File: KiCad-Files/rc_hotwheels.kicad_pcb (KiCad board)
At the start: 2 copper layers, 30 x 26 mm, 22 parts, among them IC1 BD6211F-E2, IC2 MIC5504-3.3YM5-TR, U1 STM32F070F6P6, U3 NRF24L01_Breakout

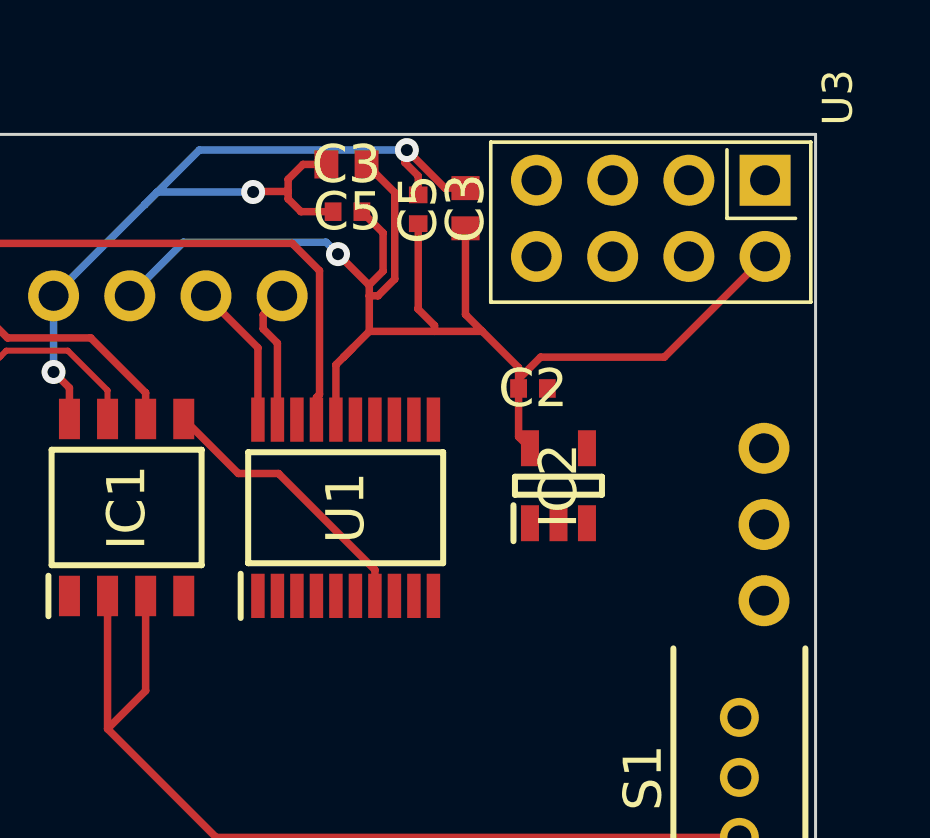
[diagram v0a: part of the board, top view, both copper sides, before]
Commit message: PCB Design
Connecting the Transceiver
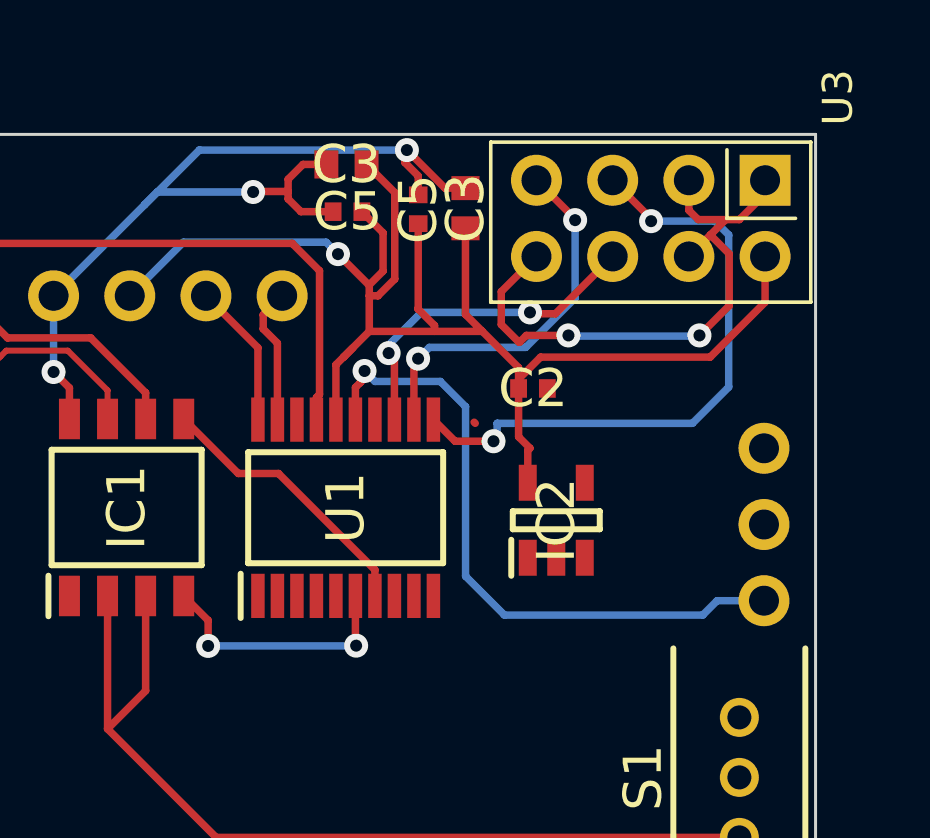
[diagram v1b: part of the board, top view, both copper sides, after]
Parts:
- moved IC2 1.15 mm to (126.0, 73.5)
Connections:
- IC1 pad 4: PA0 -> FIN
- U3 pad 5: PA5 -> SCK
- U3 pad 6: PA7 -> MOSI
- U3 pad 7: PA6 -> MISO
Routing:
- net GND: track 31.1 -> 73.0 mm, vias 3 -> 6
- net SCK: track 0.00 -> 21.0 mm, vias 0 -> 2
- net MISO: track 0.00 -> 13.0 mm, vias 0 -> 2
- net MOSI: track 0.00 -> 11.3 mm, vias 0 -> 2
- net FIN: track 0.00 -> 8.61 mm, vias 0 -> 2
- net VR_OUT: track 49.0 -> 51.0 mm

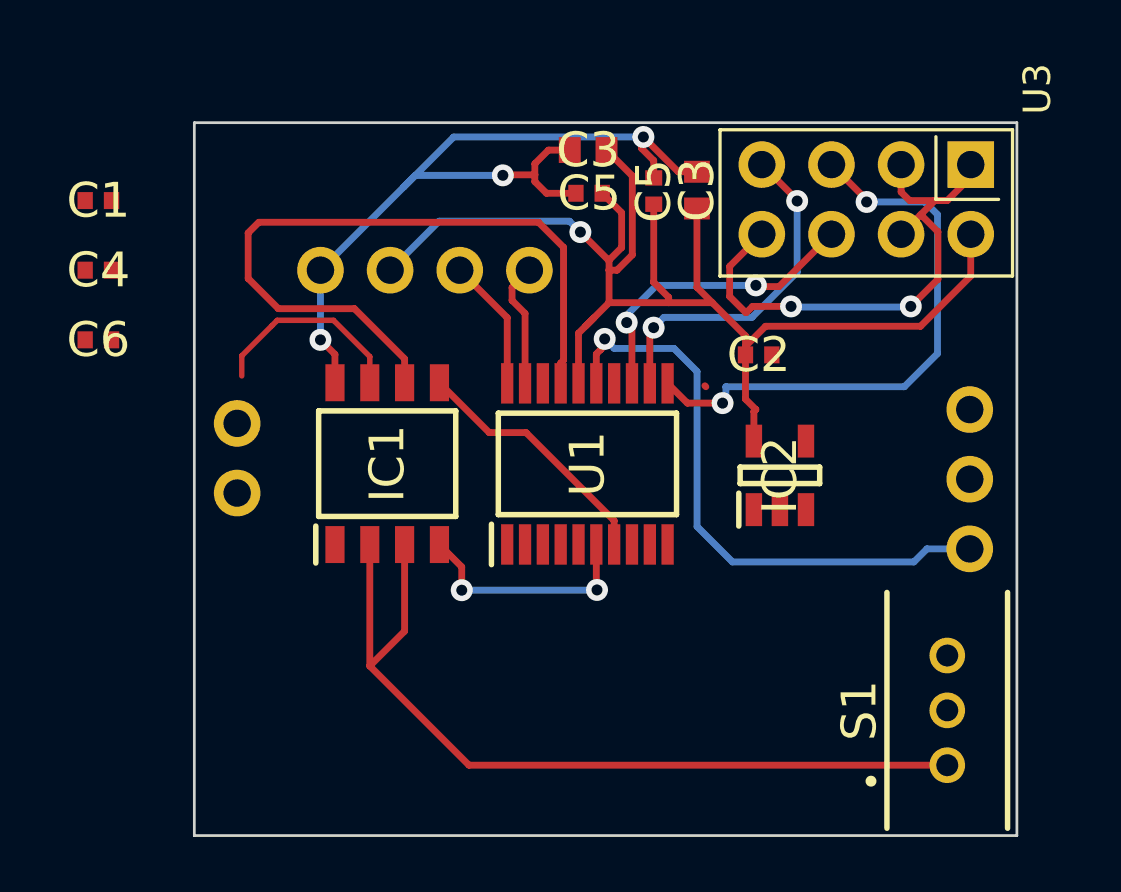
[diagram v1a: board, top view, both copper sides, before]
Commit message: Fixed all schematic errors.
Co-Authored-By: Yazid Almazroua <98489302+yazidta@users.noreply.github.com>
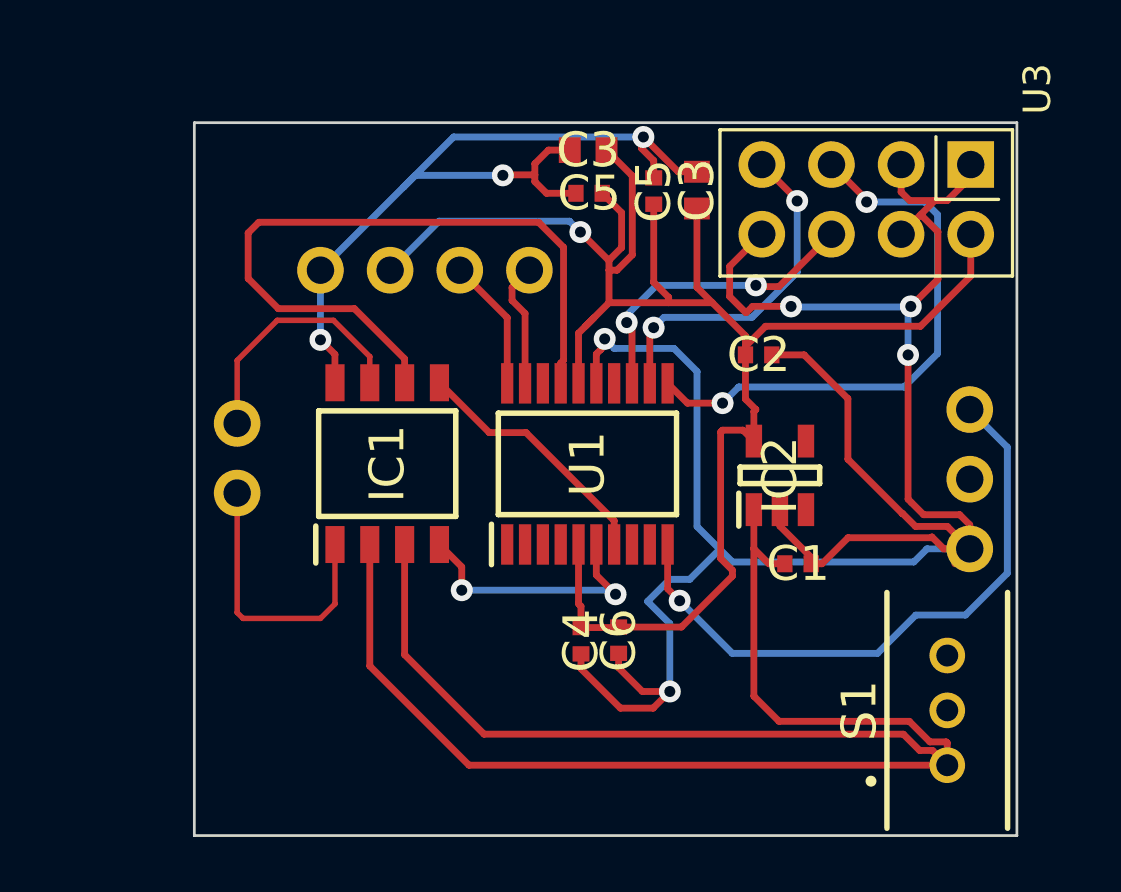
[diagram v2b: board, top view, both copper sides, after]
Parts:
- moved C1 28.8 mm to (126.6, 76.7), turned to 180 degrees
- moved C4 22.2 mm to (118.7, 79.6), turned to -90 degrees
- moved C6 21.9 mm to (120.1, 79.5), turned to 90 degrees
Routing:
- net GND: track 73.0 -> 119.1 mm, vias 6 -> 8
- net VCC: track 31.9 -> 69.2 mm
- net PWM: track 0.00 -> 22.7 mm, vias 0 -> 1
- net VR_OUT: track 51.0 -> 67.3 mm
- net Motor +: track 0.00 -> 10.4 mm
- net Motor -: track 7.44 -> 9.24 mm
- net FIN: track 8.61 -> 9.78 mm

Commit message: PCB V2.0
Co-Authored-By: Yazid Almazroua <98489302+yazidta@users.noreply.github.com>
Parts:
- removed ? (x9): , 
- removed the C3 at (123.0, 63.1)
- removed the C3 at (119.0, 61.7)
- removed the C5 at (119.0, 63.2)
- removed the C5 at (121.4, 63.2)
- added BT1: Battery_Cell, Library:Battery_Pads, F.Cu at (85.9, 51.3)
- added C3: 4.7uF, C4.7uF:CAPC1608X87N, F.Cu at (64.0, 43.7)
- added C5: 100nF, C100nF:CAPC1005X55N, F.Cu at (62.5, 43.9)
- added CH: Li-Ion 18650 battery charging, Library:Battery_Pads, F.Cu at (85.8, 56.9)
- added M1: Motor_Connection, Library:Motor_Connection, F.Cu at (85.9, 45.3)
- added SM1: Motor_Servo, Library:Servo_Motor, F.Cu at (59.8, 53.4)
- added ST: ST_Link, Library:ST_Link, F.Cu at (81.1, 35.3)
- S1: moved to B.Cu
- moved U3 76.6 mm to (60.1, 38.3), turned to 90 degrees
- moved C2 63.1 mm to (64.8, 50.7), turned to -90 degrees
- moved IC2 62.6 mm to (67.8, 50.2), turned to 180 degrees
- moved C1 61.4 mm to (71.0, 50.7), turned to -90 degrees
- moved S1 61.0 mm to (78.2, 53.3), turned to 0 degrees
- moved U1 57.9 mm to (69.0, 43.8), turned to 180 degrees
- moved C4 56.0 mm to (74.0, 46.0), turned to 90 degrees
- moved C6 55.8 mm to (75.5, 46.0), turned to -90 degrees
- moved IC1 43.5 mm to (80.6, 42.6), turned to -90 degrees
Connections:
- net VREF renamed Motor Speed
- C1 pad 1: GND -> Net-(IC2-GND)
- C2 pad 1: GND -> Net-(C2-Pad1)
- IC1 pad 4: FIN -> Motor Forward
- IC1 pad 5: RIN -> Motor Reverse
- IC2 pad 2: GND -> Net-(IC2-GND)
- S1 pad 2: +BATT -> Net-(BT1-+)
- U1 pad 6: FIN -> Motor Reverse
- U1 pad 7: RIN -> Motor Forward
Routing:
- net GND: track 119.1 -> 12.8 mm, vias 8 -> 4
- net VR_OUT: track 67.3 -> 45.2 mm, vias 1 -> 0
- net VCC: track 69.2 -> 48.9 mm
- net SCK: track 20.6 -> 2.99 mm, vias 2 -> 0
- net SYS_SWCLK: track 4.84 -> 16.8 mm
- net Motor Forward: track 0.00 -> 10.7 mm, vias 0 -> 2
- net FIN: track 9.78 -> 0.00 mm, vias 2 -> 0
- net RIN: track 9.32 -> 0.00 mm
- net Net-(BT1-+): track 0.00 -> 9.30 mm
- net SYS_SWDIO: track 4.59 -> 13.7 mm
- net Motor Reverse: track 0.00 -> 8.90 mm, vias 0 -> 2
- net MISO: track 13.0 -> 4.86 mm, vias 2 -> 0
- net Net-(S3-BATT+): track 0.00 -> 7.94 mm
- net Motor Speed: track 26.5 -> 21.9 mm, vias 0 -> 2
- net Motor +: track 10.4 -> 7.03 mm
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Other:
- board size 30 x 26 mm -> 29.5 x 23.5 mm

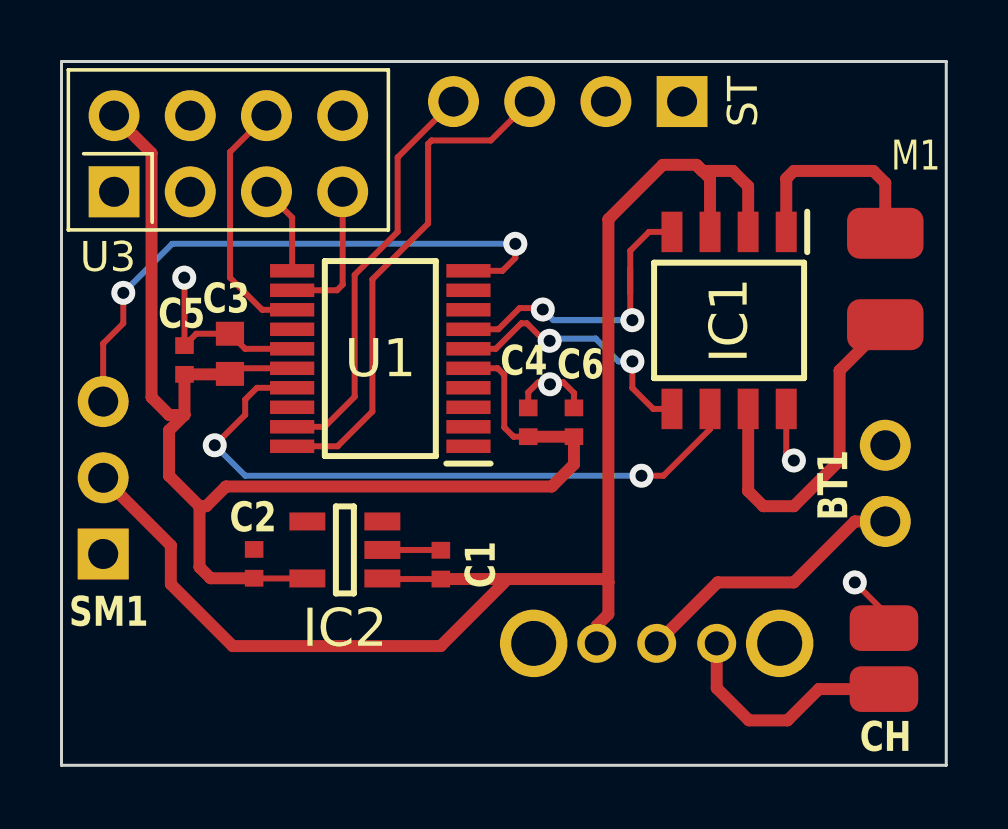
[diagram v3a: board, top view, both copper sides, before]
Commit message: Updated all power traces
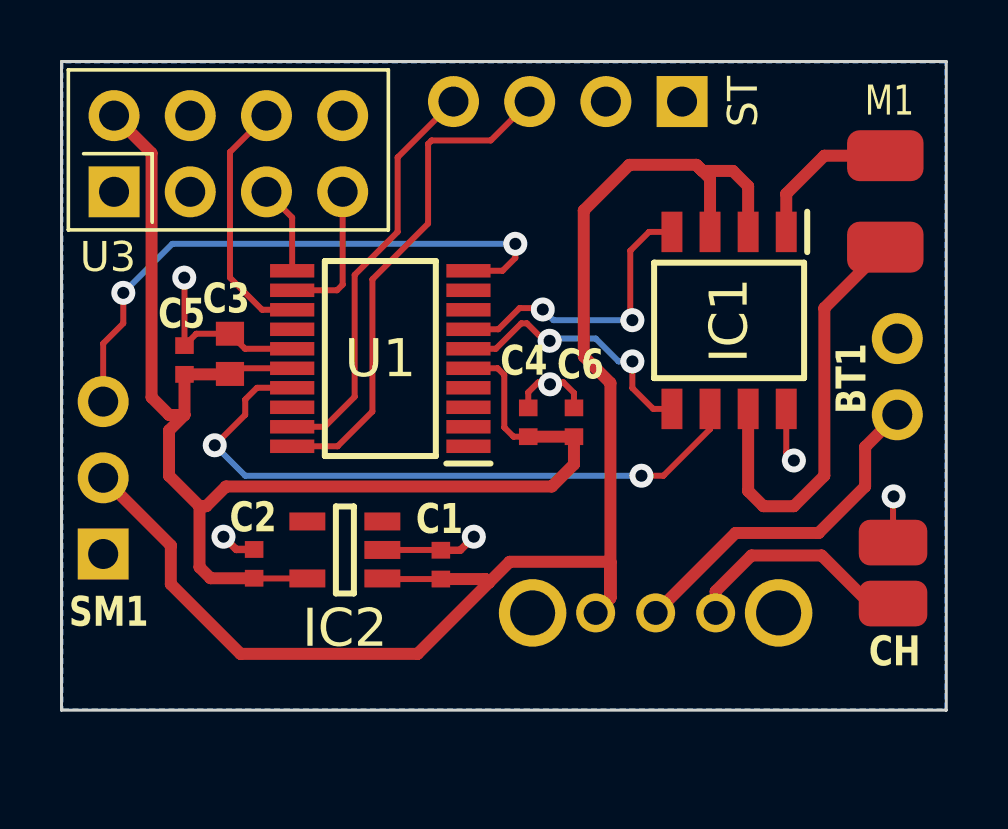
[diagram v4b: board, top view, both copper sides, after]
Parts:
- moved BT1 3.58 mm to (86.3, 47.8)
- moved CH 2.87 mm to (86.1, 54.0)
- moved M1 2.59 mm to (85.9, 42.7)
- moved S1 1.02 mm to (78.2, 52.3)
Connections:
- C1 pad 1: Net-(IC2-GND) -> GND
- C2 pad 1: Net-(C2-Pad1) -> GND
- IC2 pad 2: Net-(IC2-GND) -> GND
- SM1 pad 3: Net-(SM1--) -> GND
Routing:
- net GND: track 12.8 -> 16.9 mm, vias 4 -> 6
- net Motor -: track 11.8 -> 14.4 mm
- net Net-(BT1-+): track 9.30 -> 11.6 mm
- net Net-(IC2-GND): track 1.95 -> 0.00 mm
- net Motor +: track 7.03 -> 5.10 mm
- net VCC: track 48.9 -> 50.5 mm
- net Motor Forward: track 10.7 -> 9.92 mm
- added copper zone on B.Cu, net GND
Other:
- board size 29.5 x 23.5 mm -> 29.5 x 21.6 mm

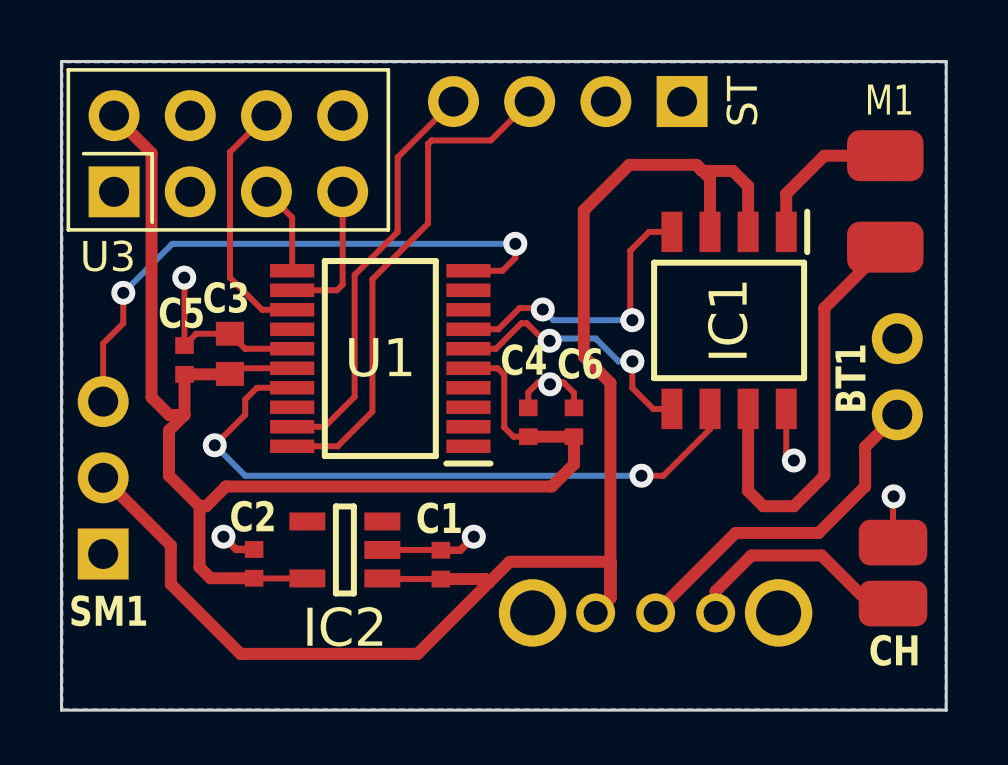
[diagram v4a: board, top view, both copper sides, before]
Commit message: Updated Capcitors libs
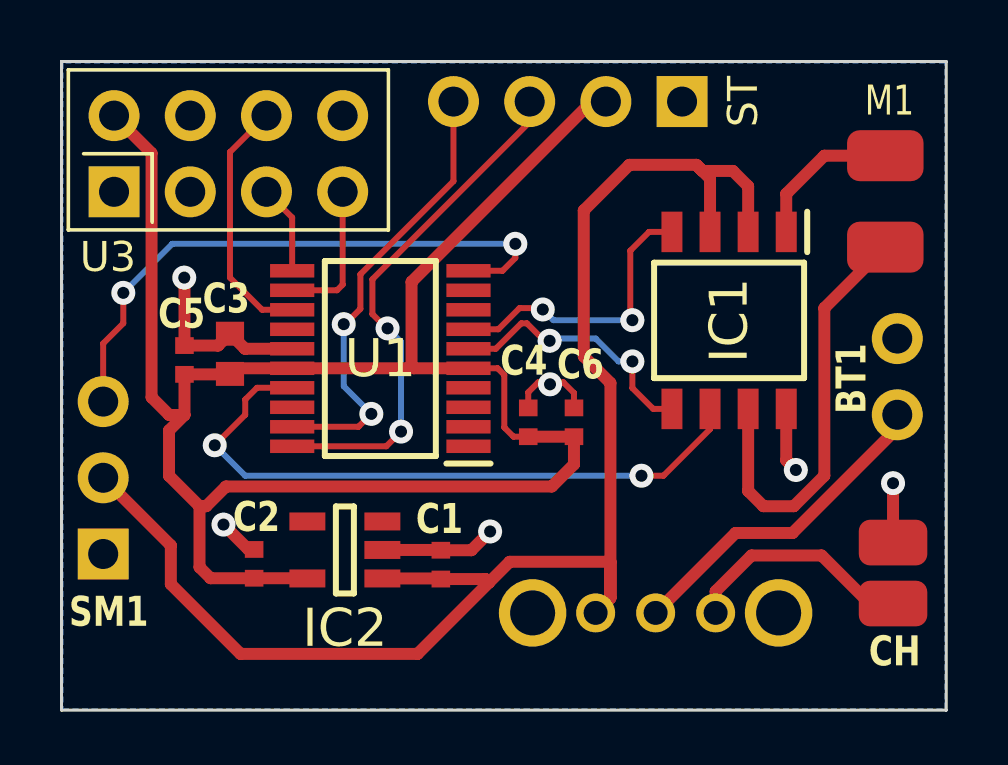
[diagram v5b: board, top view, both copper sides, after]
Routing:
- net VR_OUT: track 45.2 -> 62.9 mm
- net GND: track 16.9 -> 18.4 mm
- net SYS_SWDIO: track 13.7 -> 15.1 mm, vias 0 -> 2
- net SYS_SWCLK: track 16.8 -> 17.4 mm, vias 0 -> 2
- net Net-(BT1-+): track 11.6 -> 11.1 mm
